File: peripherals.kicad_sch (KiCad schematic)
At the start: 81 parts, among them J10 533980471, J11 ERF8-040-05.0-L-DV-K-TR, J9 TC2050-IDC-NL, Q10 NX138BKMYL, Q9 NX138BKMYL, U30 TPD4E05U06QDQARQ1, U33 NTS0102GT, U34 PCAL6408ABSHP

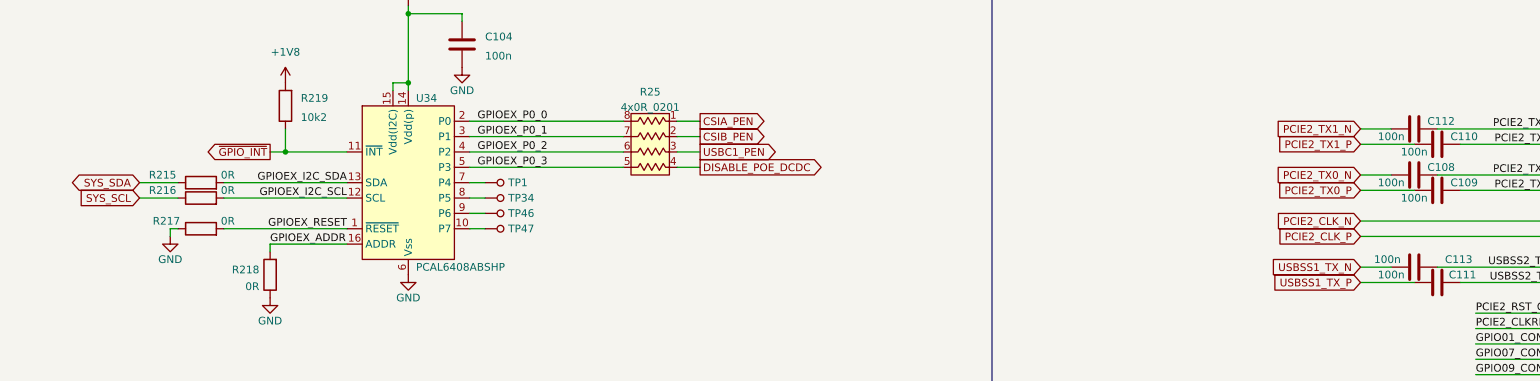
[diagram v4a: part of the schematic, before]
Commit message: CSchematic changes after review
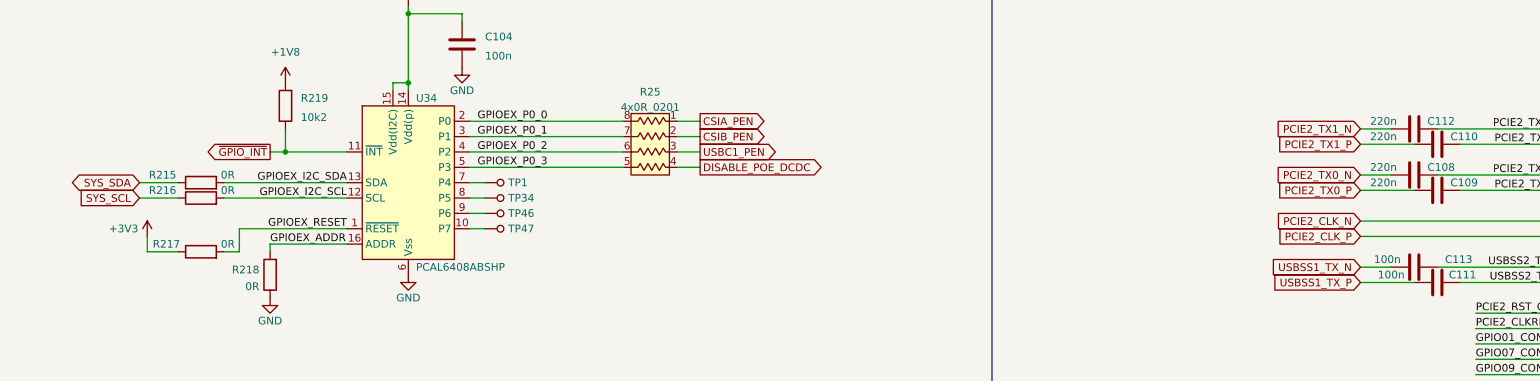
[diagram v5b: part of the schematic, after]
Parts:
- C108, C109, C110, C112: value C_100n_0402 -> C_220n_0402; symbol antmicroCapacitors0402:C_100n_0402 -> antmicroCapacitors0402:C_220n_0402; MPN GRM155R61H104KE14D -> CC0402KRX5R6BB224; Manufacturer Murata -> Yaego; Val 100n -> 220n
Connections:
- net +3V3: now also R217.1
- net GND: no longer R217.1
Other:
- moved on the sheet: R217
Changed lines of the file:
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@@
     (stroke (width 0) (type default) (color 0 0 0 0))
   )
+  (wire (pts (xy 74.93 82.55) (xy 74.93 78.74))
+    (stroke (width 0) (type default) (color 0 0 0 0))
+  )
   (wire (pts (xy 328.93 246.38) (xy 328.93 245.11))
     (stroke (width 0) (type default) (color 0 0 0 0))
@@
     (stroke (width 0) (type default) (color 0 0 0 0))
   )
-  (wire (pts (xy 64.77 78.74) (xy 63.5 78.74))
-    (stroke (width 0) (type default) (color 0 0 0 0))
-  )
   (wire (pts (xy 135.89 265.43) (xy 135.89 257.81))
     (stroke (width 0) (type default) (color 0 0 0 0))
@@
     (stroke (width 0) (type default) (color 0 0 0 0))
   )
+  (wire (pts (xy 59.69 82.55) (xy 64.77 82.55))
+    (stroke (width 0) (type default) (color 0 0 0 0))
+  )
   (wire (pts (xy 80.01 66.04) (xy 82.55 66.04))
     (stroke (width 0) (type default) (color 0 0 0 0))
@@
     (stroke (width 0) (type default) (color 0 0 0 0))
   )
+  (wire (pts (xy 74.93 78.74) (xy 92.71 78.74))
+    (stroke (width 0) (type default) (color 0 0 0 0))
+  )
   (wire (pts (xy 322.58 92.71) (xy 322.58 105.41))
     (stroke (width 0) (type default) (color 0 0 0 0))
@@
     (stroke (width 0) (type default) (color 0 0 0 0))
   )
+  (wire (pts (xy 59.69 80.01) (xy 59.69 82.55))
+    (stroke (width 0) (type default) (color 0 0 0 0))
+  )
   (wire (pts (xy 279.4 97.79) (xy 304.8 97.79))
     (stroke (width 0) (type default) (color 0 0 0 0))
@@
     (stroke (width 0) (type default) (color 0 0 0 0))
   )
+  (wire (pts (xy 72.39 82.55) (xy 74.93 82.55))
+    (stroke (width 0) (type default) (color 0 0 0 0))
+  )
   (wire (pts (xy 113.03 63.5) (xy 138.43 63.5))
     (stroke (width 0) (type default) (color 0 0 0 0))
@@
     (stroke (width 0) (type default) (color 0 0 0 0))
   )
-  (wire (pts (xy 63.5 78.74) (xy 63.5 80.01))
-    (stroke (width 0) (type default) (color 0 0 0 0))
-  )
   (wire (pts (xy 322.58 153.67) (xy 322.58 163.83))
     (stroke (width 0) (type default) (color 0 0 0 0))
@@
     (stroke (width 0) (type default) (color 0 0 0 0))
   )
-  (wire (pts (xy 72.39 78.74) (xy 92.71 78.74))
-    (stroke (width 0) (type default) (color 0 0 0 0))
-  )
   (wire (pts (xy 55.88 170.18) (xy 52.07 170.18))
     (stroke (width 0) (type default) (color 0 0 0 0))
@@
     (pin "2")
   )
-  (symbol (lib_id "antmicroCapacitors0402:C_100n_0402") (at 273.05 64.77 90) (unit 1)
+  (symbol (lib_id "antmicroCapacitors0402:C_220n_0402") (at 273.05 64.77 90) (unit 1)
     (in_bom yes) (on_board yes)
     (property "Reference" "C110" (id 0) (at 277.495 63.5 90))
-    (property "Value" "C_100n_0402" (id 1) (at 276.86 64.77 0)
-      (effects (font (size 1.27 1.27)) hide)
+    (property "Value" "C_220n_0402" (id 1) (at 276.86 64.77 0)
+      (effects (font (size 1.524 1.524)) hide)
     )
     (property "Footprint" "antmicro-footprints:0402-cap" (id 2) (at 267.97 59.69 0)
@@
       (effects (font (size 1.27 1.27)) hide)
     )
-    (property "Manufacturer" "Murata" (id 4) (at 262.89 59.69 0)
+    (property "Manufacturer" "Yaego" (id 4) (at 262.89 59.69 0)
       (effects (font (size 1.524 1.524)) (justify left) hide)
     )
-    (property "MPN" "GRM155R61H104KE14D" (id 5) (at 265.43 59.69 0)
+    (property "MPN" "CC0402KRX5R6BB224" (id 5) (at 265.43 59.69 0)
       (effects (font (size 1.524 1.524)) (justify left) hide)
     )
-    (property "Val" "100n" (id 6) (at 269.24 66.04 90))
+    (property "Val" "220n" (id 6) (at 264.16 63.5 90))
     (pin "1")
     (pin "2")
@@
     (pin "1")
   )
-  (symbol (lib_id "antmicroCapacitors0402:C_100n_0402") (at 269.24 62.23 90) (unit 1)
+  (symbol (lib_id "antmicroCapacitors0402:C_220n_0402") (at 269.24 62.23 90) (unit 1)
     (in_bom yes) (on_board yes)
     (property "Reference" "C112" (id 0) (at 273.685 60.96 90))
-    (property "Value" "C_100n_0402" (id 1) (at 273.05 62.23 0)
-      (effects (font (size 1.27 1.27)) hide)
+    (property "Value" "C_220n_0402" (id 1) (at 273.05 62.23 0)
+      (effects (font (size 1.524 1.524)) hide)
     )
     (property "Footprint" "antmicro-footprints:0402-cap" (id 2) (at 264.16 57.15 0)
@@
       (effects (font (size 1.27 1.27)) hide)
     )
-    (property "Manufacturer" "Murata" (id 4) (at 259.08 57.15 0)
+    (property "Manufacturer" "Yaego" (id 4) (at 259.08 57.15 0)
       (effects (font (size 1.524 1.524)) (justify left) hide)
     )
-    (property "MPN" "GRM155R61H104KE14D" (id 5) (at 261.62 57.15 0)
+    (property "MPN" "CC0402KRX5R6BB224" (id 5) (at 261.62 57.15 0)
       (effects (font (size 1.524 1.524)) (justify left) hide)
     )
-    (property "Val" "100n" (id 6) (at 265.43 63.5 90))
+    (property "Val" "220n" (id 6) (at 264.16 60.96 90))
     (pin "1")
     (pin "2")
@@
     (pin "8")
   )
-  (symbol (lib_id "antmicroCapacitors0402:C_100n_0402") (at 269.24 69.85 90) (unit 1)
+  (symbol (lib_id "antmicroCapacitors0402:C_220n_0402") (at 269.24 69.85 90) (unit 1)
     (in_bom yes) (on_board yes)
     (property "Reference" "C108" (id 0) (at 273.685 68.58 90))
-    (property "Value" "C_100n_0402" (id 1) (at 273.05 69.85 0)
-      (effects (font (size 1.27 1.27)) hide)
+    (property "Value" "C_220n_0402" (id 1) (at 273.05 69.85 0)
+      (effects (font (size 1.524 1.524)) hide)
     )
     (property "Footprint" "antmicro-footprints:0402-cap" (id 2) (at 264.16 64.77 0)
@@
       (effects (font (size 1.27 1.27)) hide)
     )
-    (property "Manufacturer" "Murata" (id 4) (at 259.08 64.77 0)
+    (property "Manufacturer" "Yaego" (id 4) (at 259.08 64.77 0)
       (effects (font (size 1.524 1.524)) (justify left) hide)
     )
-    (property "MPN" "GRM155R61H104KE14D" (id 5) (at 261.62 64.77 0)
+    (property "MPN" "CC0402KRX5R6BB224" (id 5) (at 261.62 64.77 0)
       (effects (font (size 1.524 1.524)) (justify left) hide)
     )
-    (property "Val" "100n" (id 6) (at 265.43 71.12 90))
+    (property "Val" "220n" (id 6) (at 264.16 68.58 90))
     (pin "1")
     (pin "2")
@@
     (pin "2")
   )
+  (symbol (lib_id "power:+3V3") (at 59.69 80.01 0) (unit 1)
+    (in_bom yes) (on_board yes)
+    (property "Reference" "#PWR0179" (id 0) (at 59.69 83.82 0)
+      (effects (font (size 1.27 1.27)) hide)
+    )
+    (property "Value" "+3V3" (id 1) (at 53.34 78.74 0)
+      (effects (font (size 1.27 1.27)) (justify left))
+    )
+    (property "Footprint" "" (id 2) (at 59.69 80.01 0)
+      (effects (font (size 1.27 1.27)) hide)
+    )
+    (property "Datasheet" "" (id 3) (at 59.69 80.01 0)
+      (effects (font (size 1.27 1.27)) hide)
+    )
+    (pin "1")
+  )
   (symbol (lib_id "antmicroResistors0402:R_200R_0402") (at 175.26 234.95 90) (unit 1)
     (in_bom yes) (on_board yes)
@@
     (pin "2")
   )
-  (symbol (lib_id "power:GND") (at 63.5 80.01 0) (mirror y) (unit 1)
-    (in_bom yes) (on_board yes) (fields_autoplaced)
-    (property "Reference" "#PWR0215" (id 0) (at 63.5 86.36 0)
-      (effects (font (size 1.27 1.27)) hide)
-    )
-    (property "Value" "GND" (id 1) (at 63.5 83.82 0))
-    (property "Footprint" "" (id 2) (at 63.5 80.01 0)
-      (effects (font (size 1.27 1.27)) hide)
-    )
-    (property "Datasheet" "" (id 3) (at 63.5 80.01 0)
-      (effects (font (size 1.27 1.27)) hide)
-    )
-    (pin "1")
-  )
-  (symbol (lib_id "antmicroResistors0402:R_0R_0402") (at 68.58 78.74 0) (unit 1)
+  (symbol (lib_id "antmicroResistors0402:R_0R_0402") (at 68.58 82.55 0) (unit 1)
     (in_bom yes) (on_board yes)
-    (property "Reference" "R217" (id 0) (at 62.865 77.47 0))
-    (property "Value" "R_0R_0402" (id 1) (at 68.58 82.55 0)
+    (property "Reference" "R217" (id 0) (at 62.865 81.28 0))
+    (property "Value" "R_0R_0402" (id 1) (at 68.58 86.36 0)
       (effects (font (size 1.27 1.27)) hide)
     )
-    (property "Footprint" "antmicro-footprints:0402-res" (id 2) (at 73.66 73.66 0)
+    (property "Footprint" "antmicro-footprints:0402-res" (id 2) (at 73.66 77.47 0)
       (effects (font (size 1.524 1.524)) (justify left) hide)
     )
-    (property "Datasheet" "" (id 3) (at 68.58 78.74 0)
+    (property "Datasheet" "" (id 3) (at 68.58 82.55 0)
       (effects (font (size 1.27 1.27)) hide)
     )
-    (property "Manufacturer" "PANASONIC" (id 4) (at 73.66 68.58 0)
+    (property "Manufacturer" "PANASONIC" (id 4) (at 73.66 72.39 0)
       (effects (font (size 1.524 1.524)) (justify left) hide)
     )
-    (property "MPN" "ERJ2GE0R00X" (id 5) (at 73.66 71.12 0)
+    (property "MPN" "ERJ2GE0R00X" (id 5) (at 73.66 74.93 0)
       (effects (font (size 1.524 1.524)) (justify left) hide)
     )
-    (property "Val" "0R" (id 6) (at 73.025 77.47 0))
+    (property "Val" "0R" (id 6) (at 73.025 81.28 0))
     (pin "1")
     (pin "2")
@@
     (pin "2")
   )
-  (symbol (lib_id "antmicroCapacitors0402:C_100n_0402") (at 273.05 72.39 90) (unit 1)
+  (symbol (lib_id "antmicroCapacitors0402:C_220n_0402") (at 273.05 72.39 90) (unit 1)
     (in_bom yes) (on_board yes)
     (property "Reference" "C109" (id 0) (at 277.495 71.12 90))
-    (property "Value" "C_100n_0402" (id 1) (at 276.86 72.39 0)
-      (effects (font (size 1.27 1.27)) hide)
+    (property "Value" "C_220n_0402" (id 1) (at 276.86 72.39 0)
+      (effects (font (size 1.524 1.524)) hide)
     )
     (property "Footprint" "antmicro-footprints:0402-cap" (id 2) (at 267.97 67.31 0)
@@
       (effects (font (size 1.27 1.27)) hide)
     )
-    (property "Manufacturer" "Murata" (id 4) (at 262.89 67.31 0)
+    (property "Manufacturer" "Yaego" (id 4) (at 262.89 67.31 0)
       (effects (font (size 1.524 1.524)) (justify left) hide)
     )
-    (property "MPN" "GRM155R61H104KE14D" (id 5) (at 265.43 67.31 0)
+    (property "MPN" "CC0402KRX5R6BB224" (id 5) (at 265.43 67.31 0)
       (effects (font (size 1.524 1.524)) (justify left) hide)
     )
-    (property "Val" "100n" (id 6) (at 269.24 73.66 90))
+    (property "Val" "220n" (id 6) (at 264.16 71.12 90))
     (pin "1")
     (pin "2")

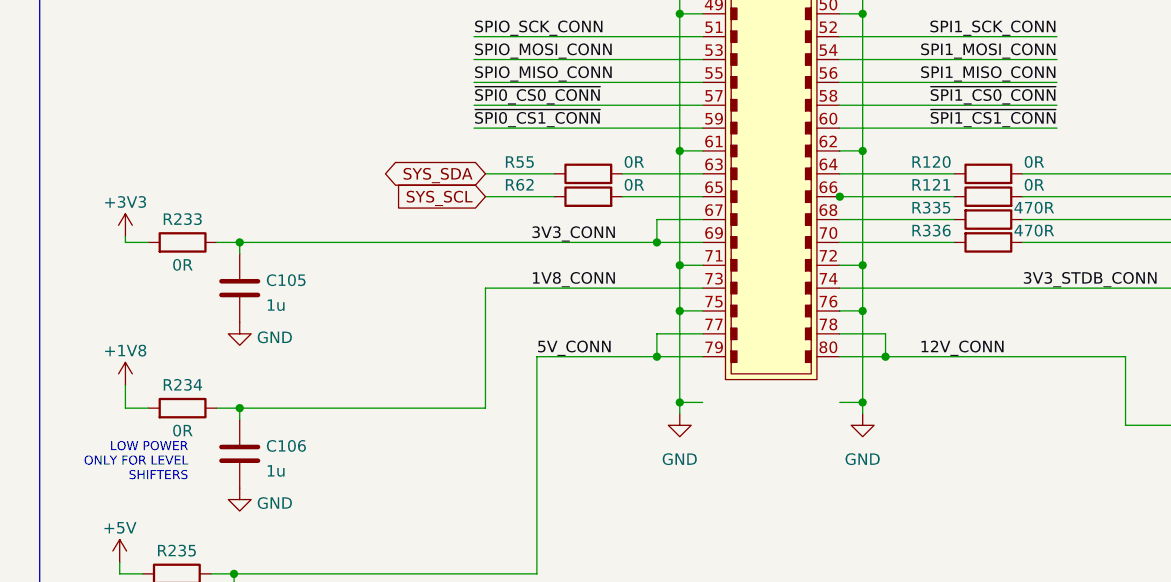
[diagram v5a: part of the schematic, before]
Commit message: Make R120, R121, R234 DNP
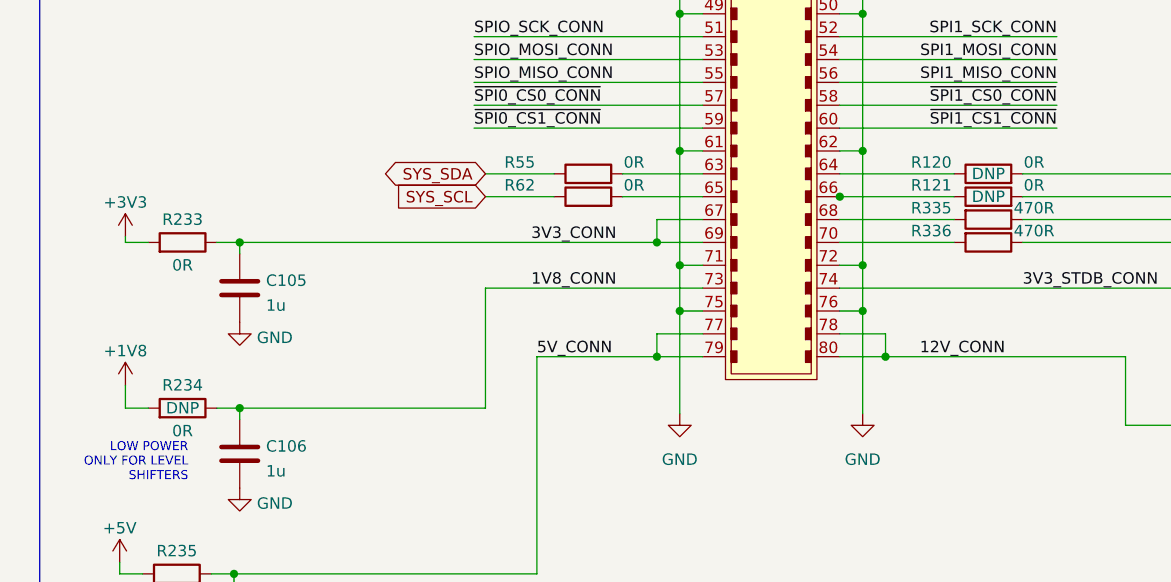
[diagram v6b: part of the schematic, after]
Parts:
- R120, R121, R234: DNP (none) -> DNP
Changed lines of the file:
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@@
     (comment 1 "www.antmicro.com")
   )
-  (junction (at 322.58 163.83) (diameter 0) (color 0 0 0 0)
-  )
   (junction (at 26.67 175.26) (diameter 0) (color 0 0 0 0)
   )
@@
   (junction (at 325.12 158.75) (diameter 0) (color 0 0 0 0)
   )
-  (junction (at 302.26 163.83) (diameter 0) (color 0 0 0 0)
-  )
   (junction (at 135.89 265.43) (diameter 0) (color 0 0 0 0)
   )
@@
     (stroke (width 0) (type default) (color 0 0 0 0))
   )
-  (wire (pts (xy 302.26 163.83) (xy 304.8 163.83))
-    (stroke (width 0) (type default) (color 0 0 0 0))
-  )
   (wire (pts (xy 224.79 191.77) (xy 198.12 191.77))
     (stroke (width 0) (type default) (color 0 0 0 0))
@@
     (stroke (width 0) (type default) (color 0 0 0 0))
   )
-  (wire (pts (xy 302.26 163.83) (xy 302.26 165.1))
-    (stroke (width 0) (type default) (color 0 0 0 0))
-  )
   (wire (pts (xy 224.79 194.31) (xy 198.12 194.31))
     (stroke (width 0) (type default) (color 0 0 0 0))
@@
     (stroke (width 0) (type default) (color 0 0 0 0))
   )
-  (wire (pts (xy 320.04 163.83) (xy 322.58 163.83))
-    (stroke (width 0) (type default) (color 0 0 0 0))
-  )
   (wire (pts (xy 396.24 204.47) (xy 398.78 204.47))
     (stroke (width 0) (type default) (color 0 0 0 0))
@@
     (stroke (width 0) (type default) (color 0 0 0 0))
   )
-  (wire (pts (xy 322.58 163.83) (xy 322.58 165.1))
-    (stroke (width 0) (type default) (color 0 0 0 0))
-  )
   (wire (pts (xy 302.26 90.17) (xy 302.26 105.41))
     (stroke (width 0) (type default) (color 0 0 0 0))
@@
     (stroke (width 0) (type default) (color 0 0 0 0))
   )
-  (wire (pts (xy 322.58 153.67) (xy 322.58 163.83))
+  (wire (pts (xy 322.58 153.67) (xy 322.58 165.1))
     (stroke (width 0) (type default) (color 0 0 0 0))
   )
@@
     (stroke (width 0) (type default) (color 0 0 0 0))
   )
-  (wire (pts (xy 302.26 153.67) (xy 302.26 163.83))
+  (wire (pts (xy 302.26 153.67) (xy 302.26 165.1))
     (stroke (width 0) (type default) (color 0 0 0 0))
   )
@@
     )
     (property "Val" "0R" (id 6) (at 247.015 167.005 0))
+    (property "DNP" "DNP" (id 7) (at 247.015 164.465 0))
     (pin "1")
     (pin "2")
@@
     )
     (property "Val" "0R" (id 6) (at 341.63 139.7 0))
+    (property "DNP" "DNP" (id 7) (at 336.55 140.97 0))
     (pin "1")
     (pin "2")
@@
     )
     (property "Val" "0R" (id 6) (at 341.63 137.16 0))
+    (property "DNP" "DNP" (id 7) (at 336.55 138.43 0))
     (pin "1")
     (pin "2")

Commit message: Loclib
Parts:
- C104, C111, C113, C44, C48: footprint antmicro-footprints:0402-cap -> jetson-orin-baseboard-footprints:0402-cap; symbol antmicroCapacitors0402:C_100n_0402 -> jetson-orin-baseboard:C_100n_0402
- C105, C106, C107, C114, C115: footprint antmicro-footprints:0402-cap -> jetson-orin-baseboard-footprints:0402-cap; symbol antmicroCapacitors0402:C_1u_0402 -> jetson-orin-baseboard:C_1u_0402
- C108, C109, C110, C112: footprint antmicro-footprints:0402-cap -> jetson-orin-baseboard-footprints:0402-cap; symbol antmicroCapacitors0402:C_220n_0402 -> jetson-orin-baseboard:C_220n_0402
- D16, D17, D19, D21, D22, D23, D39, D40, D41, D42, D43, D44, D45, D46, D47, D48, D49, D50: footprint antmicro-footprints:XDFN-2_1x0.60mm -> jetson-orin-baseboard-footprints:XDFN-2_1x0.60mm; symbol antmicroTVSDiodes:TPD1E0B04DPYR -> jetson-orin-baseboard:TPD1E0B04DPYR
- D26, D27: footprint antmicro-footprints:LED_0603 -> jetson-orin-baseboard-footprints:LED_0603; symbol antmicroLEDIndicationDiscrete:LTST-C190GKT -> jetson-orin-baseboard:LTST-C190GKT
- J10: footprint antmicro-footprints:Molex_PicoBlade_53398-0471_1x04-1MP_P1.25mm_Vertical -> jetson-orin-baseboard-footprints:Molex_PicoBlade_53398-0471_1x04-1MP_P1.25mm_Vertical; symbol antmicroRectangularConnectorsHeadersMalePins:533980471 -> jetson-orin-baseboard:533980471
- J11: footprint antmicro-footprints:ERF8-040-XX.X-X-DV-XX -> jetson-orin-baseboard-footprints:ERF8-040-XX.X-X-DV-XX; symbol antmicroB2bConnectors:ERF8-040-05.0-L-DV-K-TR -> jetson-orin-baseboard:ERF8-040-05.0-L-DV-K-TR
- J9: footprint antmicro-footprints:TC2050-IDC-NL_2x05_Vertical -> jetson-orin-baseboard-footprints:TC2050-IDC-NL_2x05_Vertical; symbol antmicroTestPoints:TC2050-IDC-NL -> jetson-orin-baseboard:TC2050-IDC-NL
- Q10, Q9: footprint antmicro-footprints:DFN1006-3 -> jetson-orin-baseboard-footprints:DFN1006-3; symbol antmicroTransistorsFETsMOSFETsSingle:NX138BKMYL -> jetson-orin-baseboard:NX138BKMYL
- R100, R101, R102, R26, R53, R54, R63, R64: footprint antmicro-footprints:R_Array_4x0402 -> jetson-orin-baseboard-footprints:R_Array_4x0402; symbol antmicroResistorNetworksArrays:4x330R_0402_array -> jetson-orin-baseboard:4x330R_0402_array
- R120, R121, R134, R141, R215, R216, R217, R218, R55, R62: footprint antmicro-footprints:0402-res -> jetson-orin-baseboard-footprints:0402-res; symbol antmicroResistors0402:R_0R_0402 -> jetson-orin-baseboard:R_0R_0402
- R219: footprint antmicro-footprints:0402-res -> jetson-orin-baseboard-footprints:0402-res; symbol antmicroResistors0402:R_10k2_0402 -> jetson-orin-baseboard:R_10k2_0402
- R222, R230: footprint antmicro-footprints:0402-res -> jetson-orin-baseboard-footprints:0402-res; symbol antmicroResistors0402:R_100k_0402 -> jetson-orin-baseboard:R_100k_0402
- R223, R231: footprint antmicro-footprints:0402-res -> jetson-orin-baseboard-footprints:0402-res; symbol antmicroResistors0402:R_200R_0402 -> jetson-orin-baseboard:R_200R_0402
- R232, R242: footprint antmicro-footprints:0402-res -> jetson-orin-baseboard-footprints:0402-res; symbol antmicroResistors0402:R_10k_0402 -> jetson-orin-baseboard:R_10k_0402
- R233, R234, R235, R247, R248: footprint antmicro-footprints:0603-res -> jetson-orin-baseboard-footprints:0603-res; symbol antmicroResistors0603:R_0R_0603 -> jetson-orin-baseboard:R_0R_0603
- R25: footprint antmicro-footprints:EXB18V -> jetson-orin-baseboard-footprints:EXB18V; symbol antmicroResistorNetworksArrays:4x0R_0201_array -> jetson-orin-baseboard:4x0R_0201_array
- R335, R336: footprint antmicro-footprints:0402-res -> jetson-orin-baseboard-footprints:0402-res; symbol antmicroResistors0402:R_470R_0402 -> jetson-orin-baseboard:R_470R_0402
- S2, S3: footprint antmicro-footprints:B3U-3000P -> jetson-orin-baseboard-footprints:B3U-3000P; symbol antmicroPushbuttonSwitches:B3U-3000PM -> jetson-orin-baseboard:B3U-3000PM
- TP1, TP34, TP46, TP47: footprint antmicro-footprints:Testpoint_smd_0_75mm -> jetson-orin-baseboard-footprints:Testpoint_smd_0_75mm; symbol antmicroTestPoints:TP_SMD_0_75MM -> jetson-orin-baseboard:TP_SMD_0_75MM
- U30: footprint antmicro-footprints:USON-10_2.5x1.0mm_P0.5mm -> jetson-orin-baseboard-footprints:USON-10_2.5x1.0mm_P0.5mm; symbol antmicroTVSDiodes:TPD4E05U06QDQARQ1 -> jetson-orin-baseboard:TPD4E05U06QDQARQ1
- U33: footprint antmicro-footprints:PSON50P100X195X50-8N -> jetson-orin-baseboard-footprints:PSON50P100X195X50-8N; symbol antmicroLogicTranslatorsLevelShifters:NTS0102GT -> jetson-orin-baseboard:NTS0102GT
- U34: footprint antmicro-footprints:VQFN-16-1EP_3x3mm -> jetson-orin-baseboard-footprints:VQFN-16-1EP_3x3mm; symbol antmicroInterfaceIOExpanders:PCAL6408ABSHP -> jetson-orin-baseboard:PCAL6408ABSHP
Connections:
- net CSIA_PEN: no longer R25.1
- net CSIB_PEN: no longer R25.2
- net DISABLE_POE_DCDC: no longer R25.4
- net GPIOEX_P0_0: no longer R25.8
- net GPIOEX_P0_1: no longer R25.7
- net GPIOEX_P0_2: no longer R25.6
- net GPIOEX_P0_3: no longer R25.5
- net USBC1_PEN: no longer R25.3
